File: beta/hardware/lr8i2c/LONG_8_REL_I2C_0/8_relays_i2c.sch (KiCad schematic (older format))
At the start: 87 parts, among them K101 G5LA-1-12VDC, K102 G5LA-1-12VDC, K103 G5LA-1-12VDC, K104 G5LA-1-12VDC, K105 G5LA-1-12VDC, K106 G5LA-1-12VDC, K107 G5LA-1-12VDC, K108 G5LA-1-12VDC, P101 CONN_3, P102 CONN_3, P103 CONN_3, P104 CONN_3, P105 CONN_3, P106 CONN_3, P107 CONN_3, P108 CONN_3, P109 CONN_2, P110 CONN_6, P112 CONN_6, P113 CONN_2, Q101 PNP, Q102 PNP, Q103 PNP, Q104 PNP, Q105 PNP, Q106 PNP, Q107 PNP, Q108 PNP, Q109 DSS20201L NPN, Q110 DSS20201L NPN, Q111 DSS20201L NPN, Q112 DSS20201L NPN, Q113 DSS20201L NPN, Q114 DSS20201L NPN, Q115 DSS20201L NPN, Q116 DSS20201L NPN, U101 PCF8574P

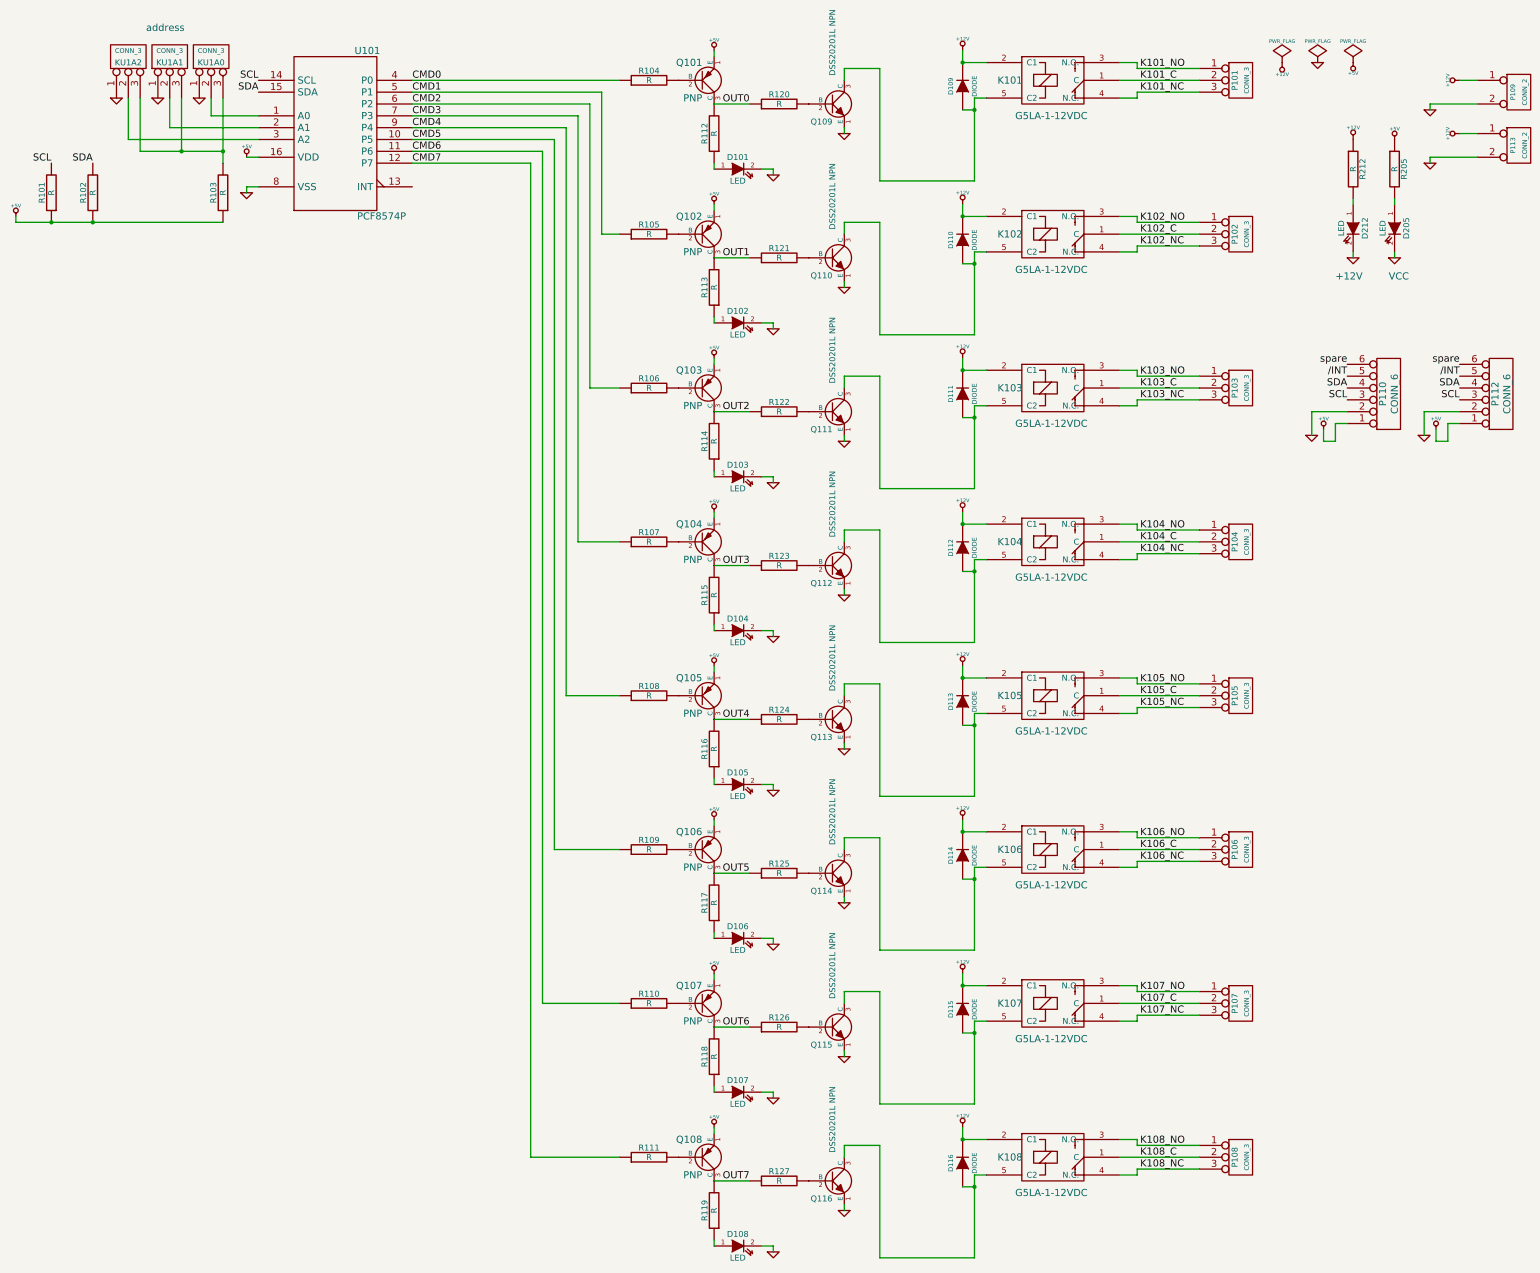
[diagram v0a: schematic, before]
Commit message: Ajout valeurs des r?sistances dans schemas (? confirmer)
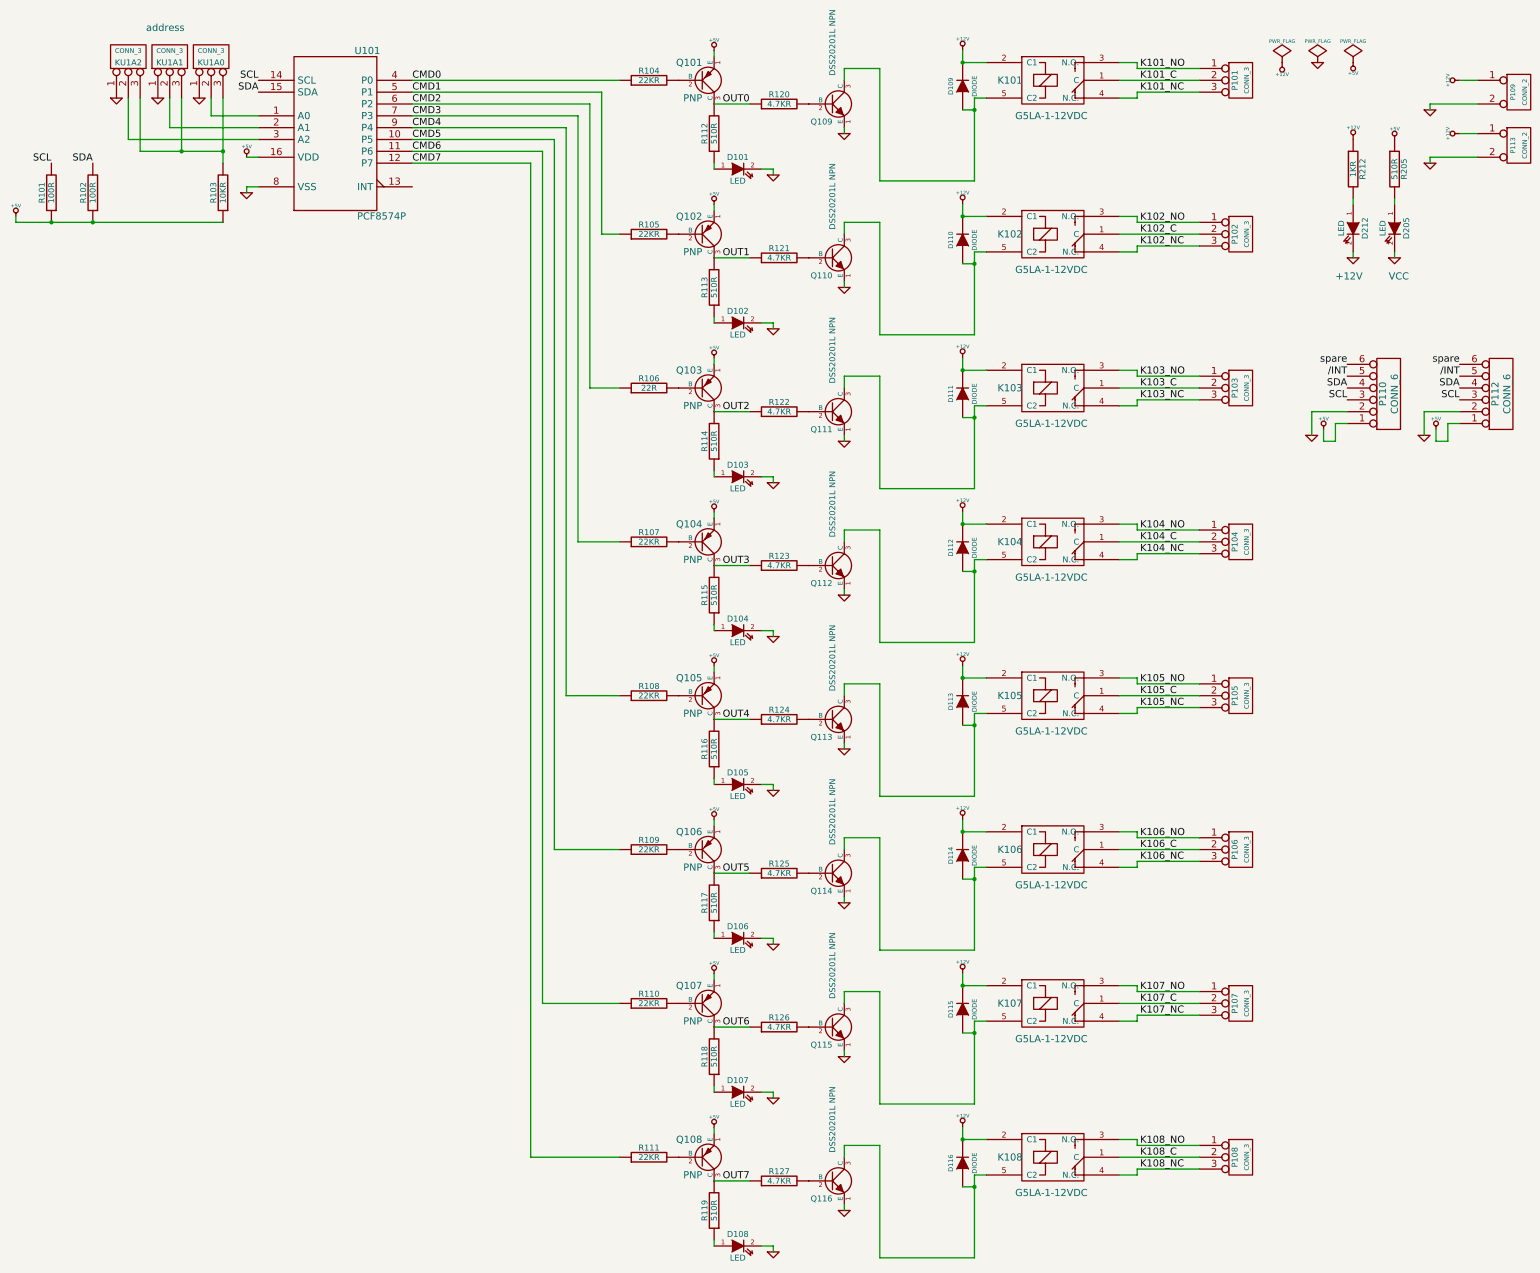
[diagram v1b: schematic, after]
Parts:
- R101, R102: value R -> 100R
- R103: value R -> 10KR
- R104, R105, R107, R108, R109, R110, R111: value R -> 22KR
- R106: value R -> 22R
- R112, R113, R114, R115, R116, R117, R118, R119, R205: value R -> 510R
- R120, R121, R122, R123, R124, R125, R126, R127: value R -> 4.7KR
- R212: value R -> 1KR
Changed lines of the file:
@@
-EESchema Schematic File Version 2  date lun. 07 mai 2012 20:59:02 CEST
+EESchema Schematic File Version 2  date ven. 18 mai 2012 21:42:45 CEST
 LIBS:power
 LIBS:device
@@
 LIBS:valves
 LIBS:g5la-1-12vdc
-LIBS:8_relays_i2c-cache
 EELAYER 25  0
 EELAYER END
@@
 Sheet 1 1
 Title ""
-Date "7 may 2012"
+Date "18 may 2012"
 Rev ""
 Comp ""
@@
 P 13650 1800
 F 0 "R205" V 13730 1800 50  0000 C CNN
-F 1 "R" V 13650 1800 50  0000 C CNN
+F 1 "510R" V 13650 1800 50  0000 C CNN
 	1    13650 1800
 	1    0    0    -1
@@
 P 13300 1800
 F 0 "R212" V 13380 1800 50  0000 C CNN
-F 1 "R" V 13300 1800 50  0000 C CNN
+F 1 "1KR" V 13300 1800 50  0000 C CNN
 	1    13300 1800
 	1    0    0    -1
@@
 P 8450 6450
 F 0 "R124" V 8530 6450 50  0000 C CNN
-F 1 "R" V 8450 6450 50  0000 C CNN
+F 1 "4.7KR" V 8450 6450 50  0000 C CNN
 	1    8450 6450
 	0    -1   -1   0
@@
 P 7900 6700
 F 0 "R116" V 7980 6700 50  0000 C CNN
-F 1 "R" V 7900 6700 50  0000 C CNN
+F 1 "510R" V 7900 6700 50  0000 C CNN
 	1    7900 6700
 	-1   0    0    1
@@
 P 7350 6250
 F 0 "R108" V 7430 6250 50  0000 C CNN
-F 1 "R" V 7350 6250 50  0000 C CNN
+F 1 "22KR" V 7350 6250 50  0000 C CNN
 	1    7350 6250
 	0    -1   -1   0
@@
 P 7350 7550
 F 0 "R109" V 7430 7550 50  0000 C CNN
-F 1 "R" V 7350 7550 50  0000 C CNN
+F 1 "22KR" V 7350 7550 50  0000 C CNN
 	1    7350 7550
 	0    -1   -1   0
@@
 P 7900 8000
 F 0 "R117" V 7980 8000 50  0000 C CNN
-F 1 "R" V 7900 8000 50  0000 C CNN
+F 1 "510R" V 7900 8000 50  0000 C CNN
 	1    7900 8000
 	-1   0    0    1
@@
 P 8450 7750
 F 0 "R125" V 8530 7750 50  0000 C CNN
-F 1 "R" V 8450 7750 50  0000 C CNN
+F 1 "4.7KR" V 8450 7750 50  0000 C CNN
 	1    8450 7750
 	0    -1   -1   0
@@
 P 8450 10350
 F 0 "R127" V 8530 10350 50  0000 C CNN
-F 1 "R" V 8450 10350 50  0000 C CNN
+F 1 "4.7KR" V 8450 10350 50  0000 C CNN
 	1    8450 10350
 	0    -1   -1   0
@@
 P 7900 10600
 F 0 "R119" V 7980 10600 50  0000 C CNN
-F 1 "R" V 7900 10600 50  0000 C CNN
+F 1 "510R" V 7900 10600 50  0000 C CNN
 	1    7900 10600
 	-1   0    0    1
@@
 P 7350 10150
 F 0 "R111" V 7430 10150 50  0000 C CNN
-F 1 "R" V 7350 10150 50  0000 C CNN
+F 1 "22KR" V 7350 10150 50  0000 C CNN
 	1    7350 10150
 	0    -1   -1   0
@@
 P 7350 8850
 F 0 "R110" V 7430 8850 50  0000 C CNN
-F 1 "R" V 7350 8850 50  0000 C CNN
+F 1 "22KR" V 7350 8850 50  0000 C CNN
 	1    7350 8850
 	0    -1   -1   0
@@
 P 7900 9300
 F 0 "R118" V 7980 9300 50  0000 C CNN
-F 1 "R" V 7900 9300 50  0000 C CNN
+F 1 "510R" V 7900 9300 50  0000 C CNN
 	1    7900 9300
 	-1   0    0    1
@@
 P 8450 9050
 F 0 "R126" V 8530 9050 50  0000 C CNN
-F 1 "R" V 8450 9050 50  0000 C CNN
+F 1 "4.7KR" V 8450 9050 50  0000 C CNN
 	1    8450 9050
 	0    -1   -1   0
@@
 P 8450 3850
 F 0 "R122" V 8530 3850 50  0000 C CNN
-F 1 "R" V 8450 3850 50  0000 C CNN
+F 1 "4.7KR" V 8450 3850 50  0000 C CNN
 	1    8450 3850
 	0    -1   -1   0
@@
 P 7900 4100
 F 0 "R114" V 7980 4100 50  0000 C CNN
-F 1 "R" V 7900 4100 50  0000 C CNN
+F 1 "510R" V 7900 4100 50  0000 C CNN
 	1    7900 4100
 	-1   0    0    1
@@
 P 7350 3650
 F 0 "R106" V 7430 3650 50  0000 C CNN
-F 1 "R" V 7350 3650 50  0000 C CNN
+F 1 "22R" V 7350 3650 50  0000 C CNN
 	1    7350 3650
 	0    -1   -1   0
@@
 P 7350 4950
 F 0 "R107" V 7430 4950 50  0000 C CNN
-F 1 "R" V 7350 4950 50  0000 C CNN
+F 1 "22KR" V 7350 4950 50  0000 C CNN
 	1    7350 4950
 	0    -1   -1   0
@@
 P 7900 5400
 F 0 "R115" V 7980 5400 50  0000 C CNN
-F 1 "R" V 7900 5400 50  0000 C CNN
+F 1 "510R" V 7900 5400 50  0000 C CNN
 	1    7900 5400
 	-1   0    0    1
@@
 P 8450 5150
 F 0 "R123" V 8530 5150 50  0000 C CNN
-F 1 "R" V 8450 5150 50  0000 C CNN
+F 1 "4.7KR" V 8450 5150 50  0000 C CNN
 	1    8450 5150
 	0    -1   -1   0
@@
 P 8450 2550
 F 0 "R121" V 8530 2550 50  0000 C CNN
-F 1 "R" V 8450 2550 50  0000 C CNN
+F 1 "4.7KR" V 8450 2550 50  0000 C CNN
 	1    8450 2550
 	0    -1   -1   0
@@
 P 7900 2800
 F 0 "R113" V 7980 2800 50  0000 C CNN
-F 1 "R" V 7900 2800 50  0000 C CNN
+F 1 "510R" V 7900 2800 50  0000 C CNN
 	1    7900 2800
 	-1   0    0    1
@@
 P 7350 2350
 F 0 "R105" V 7430 2350 50  0000 C CNN
-F 1 "R" V 7350 2350 50  0000 C CNN
+F 1 "22KR" V 7350 2350 50  0000 C CNN
 	1    7350 2350
 	0    -1   -1   0
@@
 P 3750 2000
 F 0 "R103" V 3830 2000 50  0000 C CNN
-F 1 "R" V 3750 2000 50  0000 C CNN
+F 1 "10KR" V 3750 2000 50  0000 C CNN
 	1    3750 2000
 	-1   0    0    1
@@
 P 2650 2000
 F 0 "R102" V 2730 2000 50  0000 C CNN
-F 1 "R" V 2650 2000 50  0000 C CNN
+F 1 "100R" V 2650 2000 50  0000 C CNN
 	1    2650 2000
 	-1   0    0    1
@@
 P 2300 2000
 F 0 "R101" V 2380 2000 50  0000 C CNN
-F 1 "R" V 2300 2000 50  0000 C CNN
+F 1 "100R" V 2300 2000 50  0000 C CNN
 	1    2300 2000
 	-1   0    0    1
@@
 P 7350 1050
 F 0 "R104" V 7430 1050 50  0000 C CNN
-F 1 "R" V 7350 1050 50  0000 C CNN
+F 1 "22KR" V 7350 1050 50  0000 C CNN
 	1    7350 1050
 	0    -1   -1   0
@@
 P 7900 1500
 F 0 "R112" V 7980 1500 50  0000 C CNN
-F 1 "R" V 7900 1500 50  0000 C CNN
+F 1 "510R" V 7900 1500 50  0000 C CNN
 	1    7900 1500
 	-1   0    0    1
@@
 P 8450 1250
 F 0 "R120" V 8530 1250 50  0000 C CNN
-F 1 "R" V 8450 1250 50  0000 C CNN
+F 1 "4.7KR" V 8450 1250 50  0000 C CNN
 	1    8450 1250
 	0    -1   -1   0
